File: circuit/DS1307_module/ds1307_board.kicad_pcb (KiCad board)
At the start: 2 copper layers, 5 parts, among them P1 CONN_4, U1 DS1307, X1 CRYSTAL

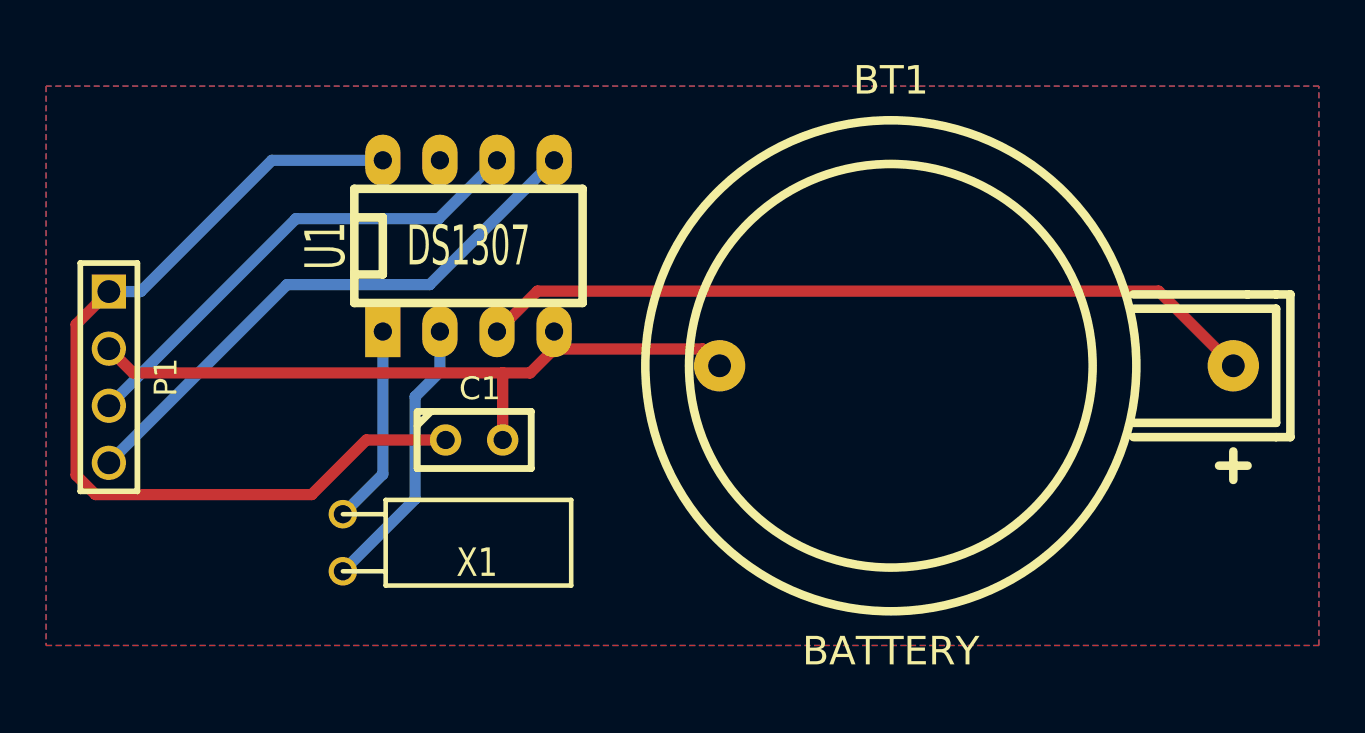
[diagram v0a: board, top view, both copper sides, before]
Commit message: DS1307 board: Add some logo
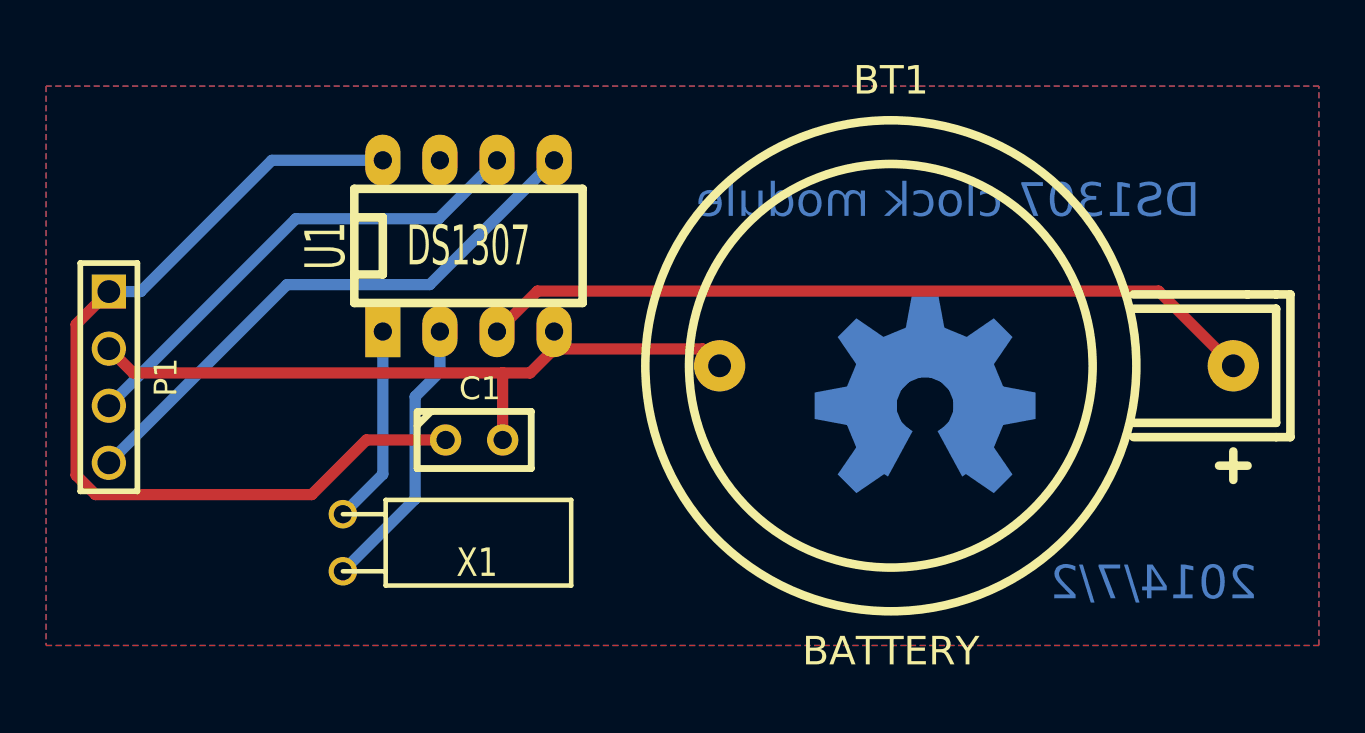
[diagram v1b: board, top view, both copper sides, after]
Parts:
- added OSHW_COPPER_10MM: VAL**, OSHW_COPPER_10MM, B.Cu at (159.3, 108.0)
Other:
- board text added: "2014/7/2"
- board text added: "DS1307 clock module"
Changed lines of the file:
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@@
     (area 119.3864 92.1576 176.784001 120.1864)
     (thickness 1.6)
-    (drawings 0)
+    (drawings 2)
     (tracks 32)
     (zones 0)
-    (modules 5)
+    (modules 6)
     (nets 9)
   )
@@
     (add_net SDA)
   )
+  (module OSHW_COPPER_10MM (layer B.Cu)
+    (at 159.258 107.95 180)
+    (fp_text reference OSHW_COPPER_10MM (at 0 0 180) (layer B.SilkS) hide
+      (effects (font (thickness 0.3048)) (justify mirror))
+    )
+    (fp_text value VAL** (at 0 0 180) (layer B.SilkS) hide
+      (effects (font (thickness 0.3048)) (justify mirror))
+    )
+    (pad "" smd trapezoid (at 0 4.1656) (size 1.45796 1.4986) (rect_delta 0 0.2794 )
+      (layers B.Cu B.Paste B.Mask)
+    )
+    (pad "" smd trapezoid (at 2.94386 2.94386 45) (size 1.45796 1.4986) (rect_delta 0 0.2794 )
+      (layers B.Cu B.Paste B.Mask)
+    )
+    (pad "" smd trapezoid (at 4.1656 0 90) (size 1.45796 1.4986) (rect_delta 0 0.2794 )
+      (layers B.Cu B.Paste B.Mask)
+    )
+    (pad "" smd trapezoid (at 2.94386 -2.94386 135) (size 1.45796 1.4986) (rect_delta 0 0.2794 )
+      (layers B.Cu B.Paste B.Mask)
+    )
+    (pad "" smd trapezoid (at -2.94386 2.94386 315) (size 1.45796 1.4986) (rect_delta 0 0.2794 )
+      (layers B.Cu B.Paste B.Mask)
+    )
+    (pad "" smd trapezoid (at -4.1656 0 270) (size 1.45796 1.4986) (rect_delta 0 0.2794 )
+      (layers B.Cu B.Paste B.Mask)
+    )
+    (pad "" smd trapezoid (at -2.94386 -2.94386 225) (size 1.45796 1.4986) (rect_delta 0 0.2794 )
+      (layers B.Cu B.Paste B.Mask)
+    )
+    (pad "" smd trapezoid (at 0 2.39522) (size 1.08204 2.29108) (rect_delta 0 -0.41402 )
+      (layers B.Cu B.Paste B.Mask)
+    )
+    (pad "" smd trapezoid (at -0.9144 2.21234 337.5) (size 1.08204 2.29108) (rect_delta 0 -0.41402 )
+      (layers B.Cu B.Paste B.Mask)
+    )
+    (pad "" smd trapezoid (at 0.9144 2.21234 22.5) (size 1.08204 2.29108) (rect_delta 0 -0.41402 )
+      (layers B.Cu B.Paste B.Mask)
+    )
+    (pad "" smd trapezoid (at 1.69164 1.69164 45) (size 1.08204 2.29108) (rect_delta 0 -0.41402 )
+      (layers B.Cu B.Paste B.Mask)
+    )
+    (pad "" smd trapezoid (at -1.69164 1.69164 315) (size 1.08204 2.29108) (rect_delta 0 -0.41402 )
+      (layers B.Cu B.Paste B.Mask)
+    )
+    (pad "" smd trapezoid (at 2.21234 0.9144 67.5) (size 1.08204 2.29108) (rect_delta 0 -0.41402 )
+      (layers B.Cu B.Paste B.Mask)
+    )
+    (pad "" smd trapezoid (at -2.21234 0.9144 292.5) (size 1.08204 2.29108) (rect_delta 0 -0.41402 )
+      (layers B.Cu B.Paste B.Mask)
+    )
+    (pad "" smd trapezoid (at 2.39522 0 90) (size 1.08204 2.29108) (rect_delta 0 -0.41402 )
+      (layers B.Cu B.Paste B.Mask)
+    )
+    (pad "" smd trapezoid (at -2.39522 0 270) (size 1.08204 2.29108) (rect_delta 0 -0.41402 )
+      (layers B.Cu B.Paste B.Mask)
+    )
+    (pad "" smd trapezoid (at -2.21234 -0.9144 247.5) (size 1.08204 2.29108) (rect_delta 0 -0.41402 )
+      (layers B.Cu B.Paste B.Mask)
+    )
+    (pad "" smd trapezoid (at 2.21234 -0.9144 112.5) (size 1.08204 2.29108) (rect_delta 0 -0.41402 )
+      (layers B.Cu B.Paste B.Mask)
+    )
+    (pad "" smd trapezoid (at 1.69164 -1.69164 135) (size 1.08204 2.29108) (rect_delta 0 -0.41402 )
+      (layers B.Cu B.Paste B.Mask)
+    )
+    (pad "" smd trapezoid (at -1.69164 -1.69164 225) (size 1.08204 2.29108) (rect_delta 0 -0.41402 )
+      (layers B.Cu B.Paste B.Mask)
+    )
+    (pad "" smd trapezoid (at -1.32842 -1.99136 213.7) (size 0.54102 2.29108) (rect_delta 0 -0.20828 )
+      (layers B.Cu B.Paste B.Mask)
+    )
+    (pad "" smd trapezoid (at 1.32842 -1.99136 146.3) (size 0.54102 2.29108) (rect_delta 0 -0.20828 )
+      (layers B.Cu B.Paste B.Mask)
+    )
+  )
   (module CR2032H (layer F.Cu)
     (at 157.734 106.172)
@@
     )
   )
+  (gr_text "DS1307 clock module" (at 160.274 98.806) (layer B.Cu)
+    (effects (font (size 1.5 1.5) (thickness 0.3)) (justify mirror))
+  )
+  (gr_text "2014/7/2\n" (at 169.418 115.824) (layer B.Cu)
+    (effects (font (size 1.5 1.5) (thickness 0.3)) (justify mirror))
+  )
   (segment (start 130.1903 97.028) (end 124.3483 102.87) (width 0.5) (layer B.Cu) (net 1))

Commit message: DS1307 board: Add the board edge
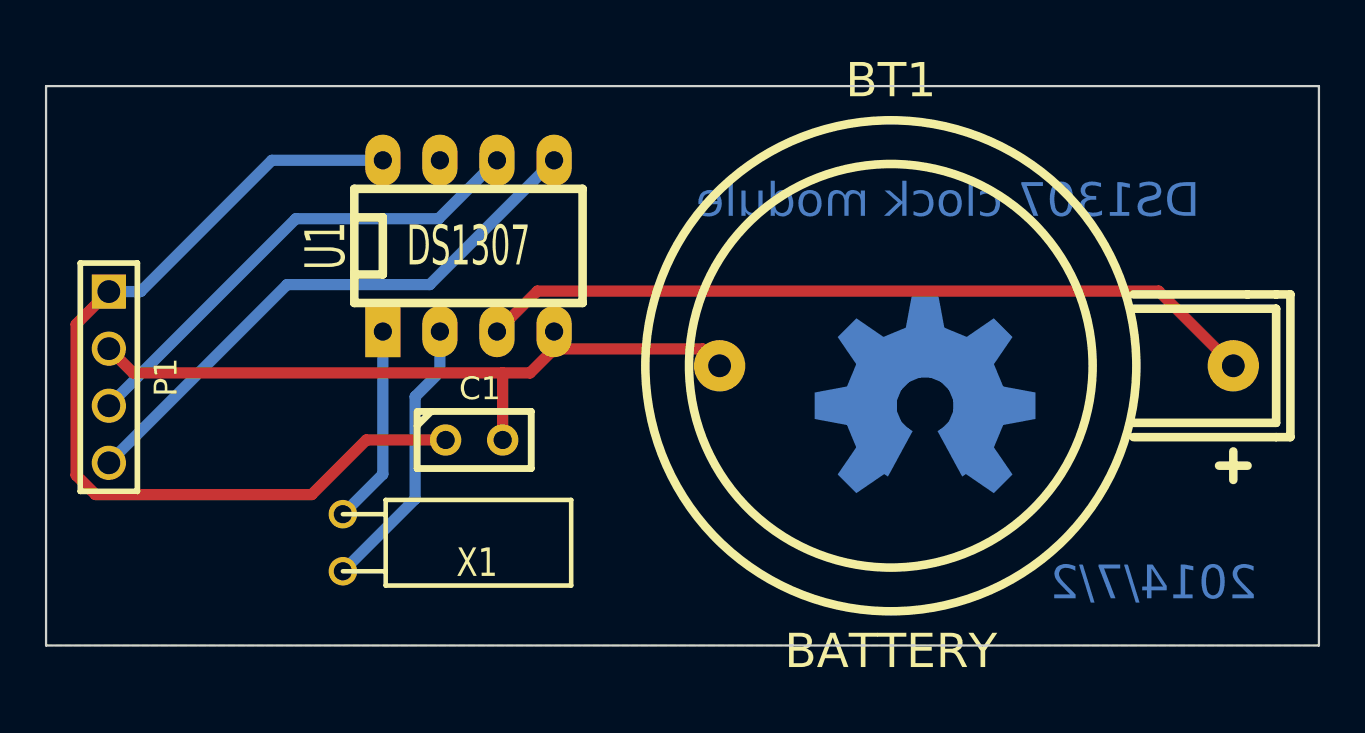
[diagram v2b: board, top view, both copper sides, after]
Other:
- board outline added: 56.6 x 24.9 mm
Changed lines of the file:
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@@
-(kicad_pcb (version 3) (host pcbnew "(2013-mar-13)-testing")
+(kicad_pcb (version 3) (host pcbnew "(2013-jul-07)-stable")
   (general
     (links 10)
     (no_connects 0)
-    (area 119.3864 92.1576 176.784001 120.1864)
+    (area 119.3864 92.1576 176.834001 120.1864)
     (thickness 1.6)
-    (drawings 2)
+    (drawings 6)
     (tracks 32)
     (zones 0)
@@
     (at 159.258 107.95 180)
     (fp_text reference OSHW_COPPER_10MM (at 0 0 180) (layer B.SilkS) hide
-      (effects (font (thickness 0.3048)) (justify mirror))
+      (effects (font (size 1.524 1.524) (thickness 0.3048)) (justify mirror))
     )
     (fp_text value VAL** (at 0 0 180) (layer B.SilkS) hide
-      (effects (font (thickness 0.3048)) (justify mirror))
+      (effects (font (size 1.524 1.524) (thickness 0.3048)) (justify mirror))
     )
     (pad "" smd trapezoid (at 0 4.1656) (size 1.45796 1.4986) (rect_delta 0 0.2794 )
@@
     (at 157.734 106.172)
     (fp_text reference BT1 (at 0 -12.7) (layer F.SilkS)
-      (effects (font (thickness 0.3048)))
+      (effects (font (size 1.524 1.524) (thickness 0.3048)))
     )
     (fp_text value BATTERY (at 0 12.7) (layer F.SilkS)
-      (effects (font (thickness 0.3048)))
+      (effects (font (size 1.524 1.524) (thickness 0.3048)))
     )
     (fp_line (start 15.24 3.81) (end 15.24 5.08) (layer F.SilkS) (width 0.381))
@@
     )
   )
+  (gr_line (start 120.142 93.726) (end 176.784 93.726) (angle 90) (layer Edge.Cuts) (width 0.1))
+  (gr_line (start 120.142 118.618) (end 120.142 93.726) (angle 90) (layer Edge.Cuts) (width 0.1))
+  (gr_line (start 176.784 118.618) (end 120.142 118.618) (angle 90) (layer Edge.Cuts) (width 0.1))
+  (gr_line (start 176.784 93.726) (end 176.784 118.618) (angle 90) (layer Edge.Cuts) (width 0.1))
   (gr_text "DS1307 clock module" (at 160.274 98.806) (layer B.Cu)
     (effects (font (size 1.5 1.5) (thickness 0.3)) (justify mirror))

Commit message: DS1307 board: Remove the coper zone, adjust the track line
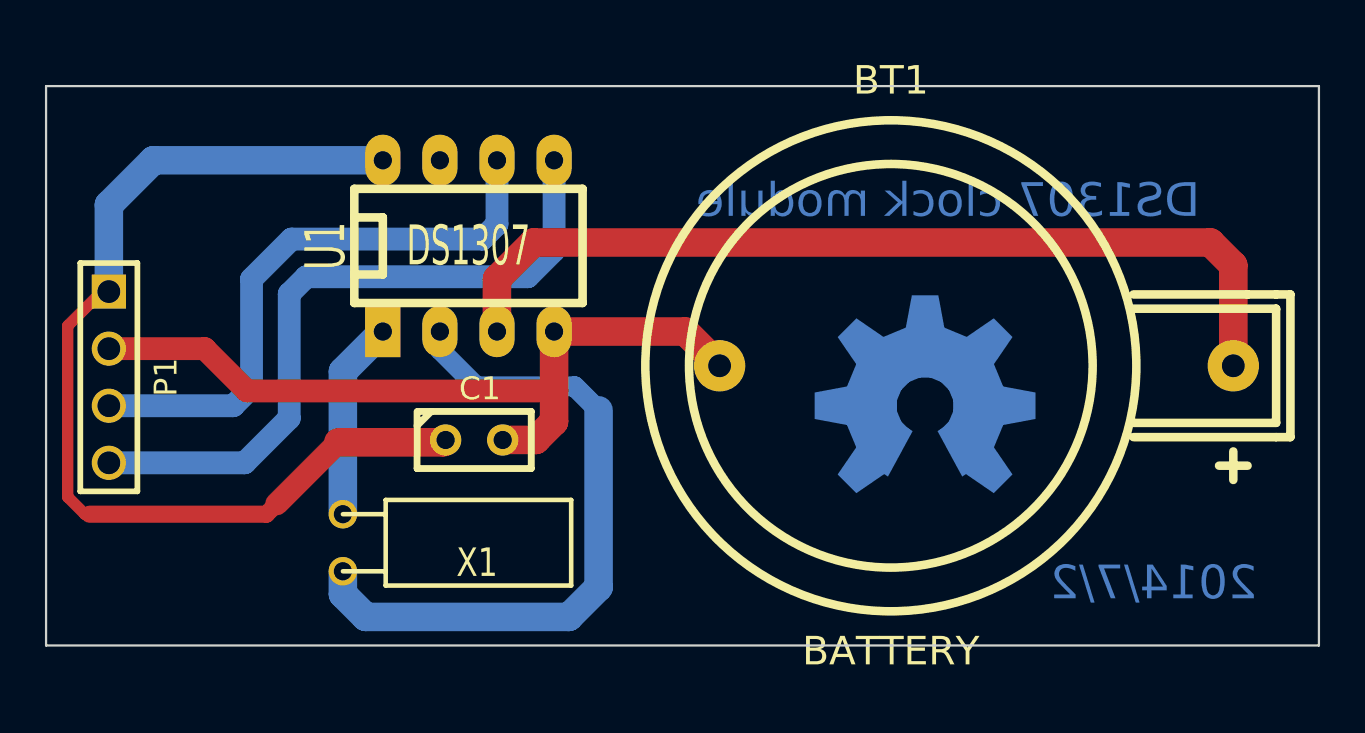
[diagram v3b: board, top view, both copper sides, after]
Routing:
- net N-000001: track 12.5 -> 60.7 mm
- net 5V: track 41.2 -> 64.3 mm
- net N-000005: track 34.9 -> 40.7 mm
- net SDA: track 25.4 -> 31.0 mm
- net GND: track 32.1 -> 37.1 mm
- net SCL: track 21.8 -> 26.3 mm
- removed copper zone on B.Cu, net (none)
- removed copper zone on F.Cu, net (none)

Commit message: DS1307 board: Optimize the layout
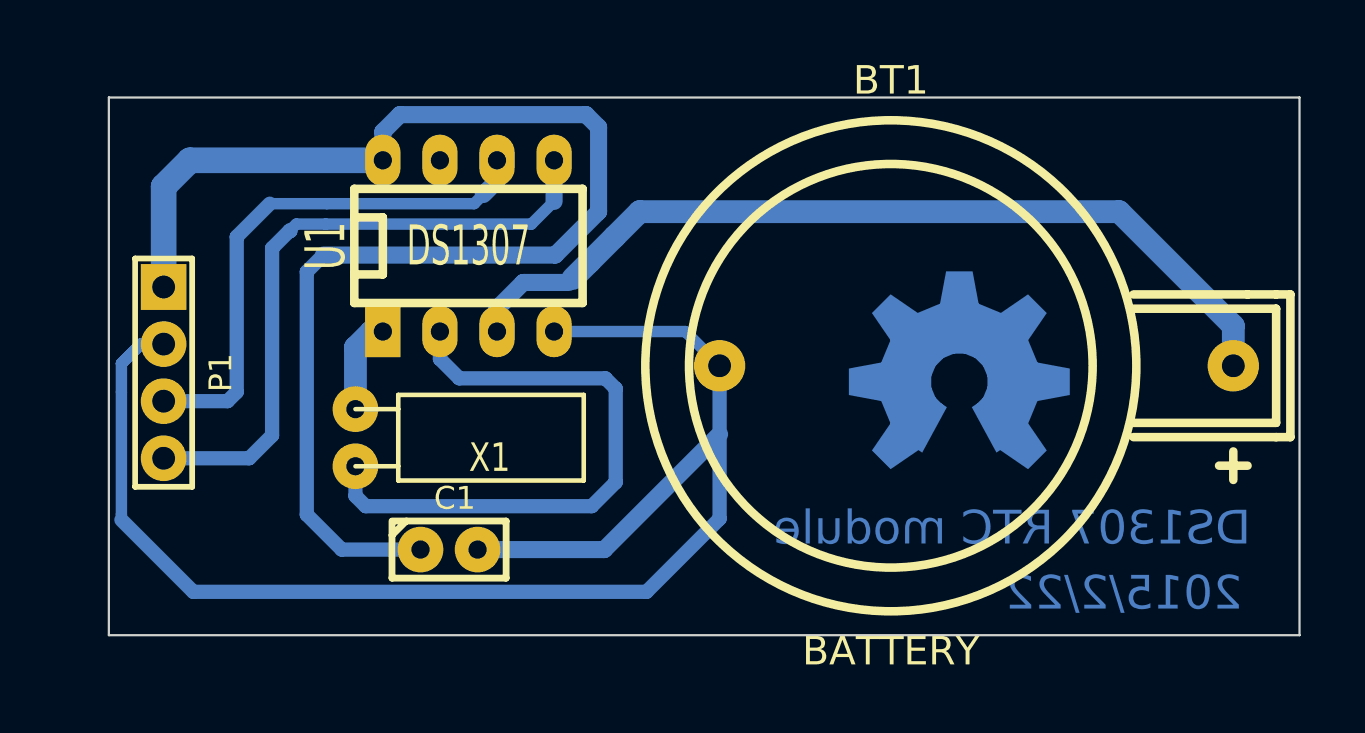
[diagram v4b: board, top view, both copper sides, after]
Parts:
- moved C1 5.00 mm to (138.1, 114.4)
- moved X1 4.71 mm to (133.9, 109.4)
- moved P1 2.45 mm to (125.4, 106.5)
- moved OSHW_COPPER_10MM 1.86 mm to (160.8, 106.9)
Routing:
- net GND: track 37.1 -> 75.7 mm
- net N-000001: track 60.7 -> 27.3 mm
- net N-000007: track 8.86 -> 4.26 mm
- net 5V: track 64.3 -> 67.3 mm
- net SCL: track 26.3 -> 24.7 mm
- net SDA: track 31.0 -> 30.0 mm
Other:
- board size 56.6 x 24.9 mm -> 53 x 23.9 mm
- board text added: "2015/2/22"
- board text added: "DS1307 RTC module"
- board text removed: "2014/7/2"
- board text removed: "DS1307 clock module"

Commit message: DS1307 board: Add a new label
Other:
- board text added: "Beware of the EMI"
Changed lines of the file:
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@@
     (area 119.357372 91.548 176.104501 120.4912)
     (thickness 1.6)
-    (drawings 6)
+    (drawings 7)
     (tracks 79)
     (zones 0)
@@
     )
   )
+  (gr_text "Beware of the EMI" (at 164.1348 96.5708) (layer B.Cu)
+    (effects (font (size 1.5 1.5) (thickness 0.3)) (justify mirror))
+  )
   (gr_line (start 122.936 118.1608) (end 122.936 94.234) (angle 90) (layer Edge.Cuts) (width 0.1))

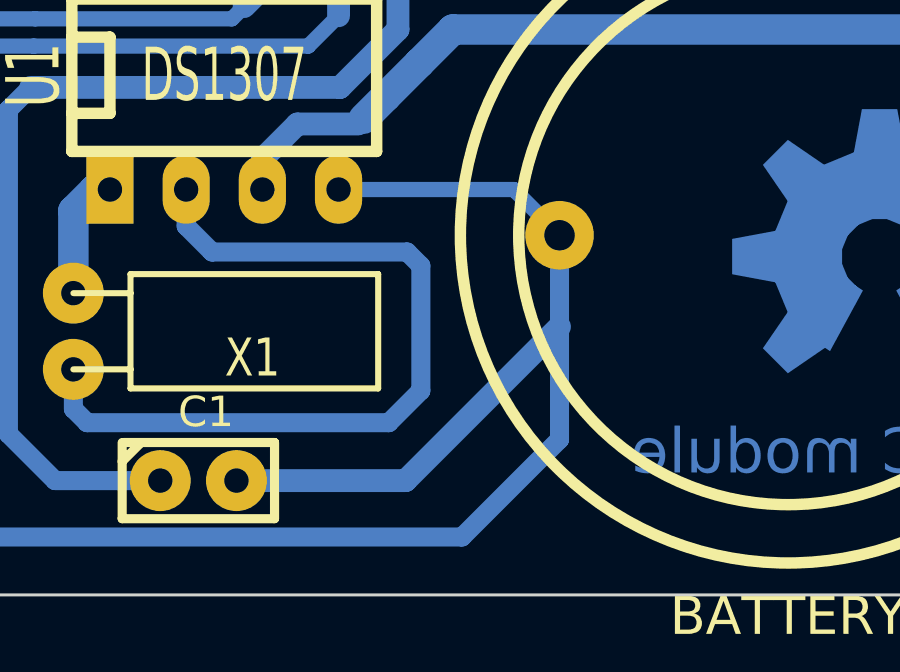
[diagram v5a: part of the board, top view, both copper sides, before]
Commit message: DS1307 module: Optimize the layout to only single side
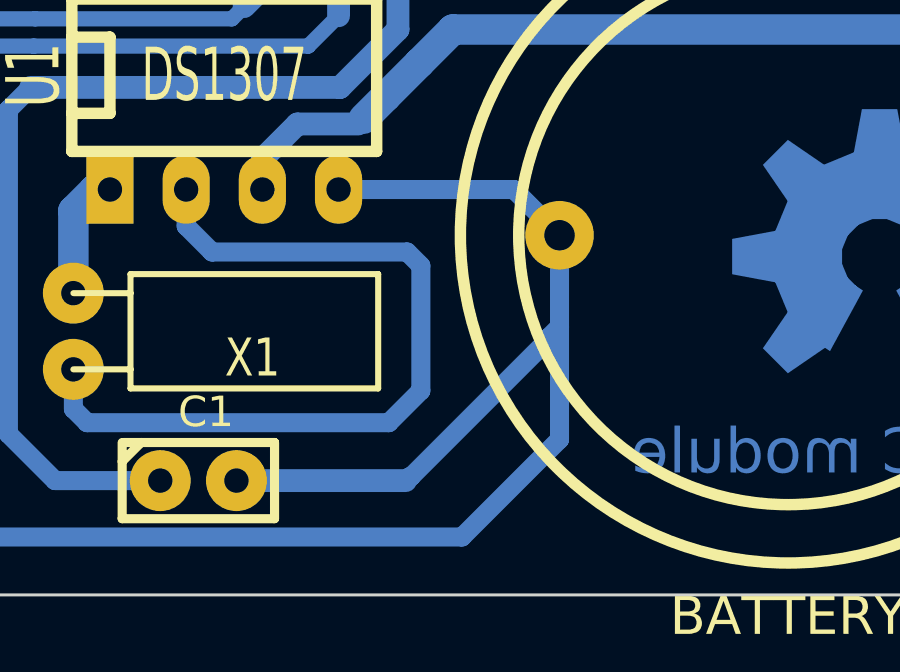
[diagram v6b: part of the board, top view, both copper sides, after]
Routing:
- net GND: track 75.7 -> 70.6 mm
